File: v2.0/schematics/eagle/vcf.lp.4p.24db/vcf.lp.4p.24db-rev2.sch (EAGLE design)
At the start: 83 parts, among them IC1 TL082P, IC2 TL084P, IC3 TL084P, IC4 LM13700N, IC5 LM13700N, J1 IN, J2 OUT, T1 2N3904, T2 2N3904, T3 2N3906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

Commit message: VCFLP - updated rev3 with zenner clipping
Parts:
- added D2, D3: 1N5232B, _common:1N5232B
- R25: value 27K -> 100K
- R27: value 10K -> 68K
- RV3: value 10K (B) -> 250K (B)
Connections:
- new net N$35: D2.C, D3.C
- net 0V: now also D3.A
- net N$47: now also D2.A
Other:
- note added: "Alternative: R27 = 3.3K, RV3 = 10K"
- note added: "CUTOFF INIT"
- note added: "Option: - Res Boost switch isn't really that useful -- Hardwire res in to IC2D pin 14 (max res) - Use switch to select 4 pole / 2 pole -- Switch C12 between IC3A pin 1 and IC3C pin 8"
- note added: "Option: Add attenuverter"
- note removed: "ADD ATTENUVERTER"
- note removed: "Add trimmer to R16 (20K) to boost up to 25K to clip resonance overload"
- note removed: "FREQ INIT"
- note removed: "May want to set R8 to 200K, and boost the output R43 to 200K"
- note removed: "Note: The board traces need to be swapped for the cuttoff pins 2 and 3. Even though th schem is correct, the board mapping seems to have been broken for these two pins."
- note removed: "R27 to 3.3K (or 68K with VB3 at 250K) R25 to 100K Pair of Zenners from pin 7 to 0V to introduce clipping on REZ."
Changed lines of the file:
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@@
 <grid distance="0.1" unitdist="inch" unit="inch" style="lines" multiple="1" display="no" altdistance="0.01" altunitdist="inch" altunit="inch"/>
 <layers>
-<layer number="1" name="Top" color="4" fill="1" visible="no" active="no"/>
-<layer number="16" name="Bottom" color="1" fill="1" visible="no" active="no"/>
-<layer number="17" name="Pads" color="2" fill="1" visible="no" active="no"/>
-<layer number="18" name="Vias" color="2" fill="1" visible="no" active="no"/>
-<layer number="19" name="Unrouted" color="6" fill="1" visible="no" active="no"/>
-<layer number="20" name="Dimension" color="24" fill="1" visible="no" active="no"/>
-<layer number="21" name="tPlace" color="7" fill="1" visible="no" active="no"/>
-<layer number="22" name="bPlace" color="7" fill="1" visible="no" active="no"/>
-<layer number="23" name="tOrigins" color="15" fill="1" visible="no" active="no"/>
-<layer number="24" name="bOrigins" color="15" fill="1" visible="no" active="no"/>
-<layer number="25" name="tNames" color="7" fill="1" visible="no" active="no"/>
-<layer number="26" name="bNames" color="7" fill="1" visible="no" active="no"/>
-<layer number="27" name="tValues" color="7" fill="1" visible="no" active="no"/>
-<layer number="28" name="bValues" color="7" fill="1" visible="no" active="no"/>
+<layer number="1" name="Top" color="4" fill="1" visible="yes" active="no"/>
+<layer number="16" name="Bottom" color="1" fill="1" visible="yes" active="no"/>
+<layer number="17" name="Pads" color="2" fill="1" visible="yes" active="no"/>
+<layer number="18" name="Vias" color="2" fill="1" visible="yes" active="no"/>
+<layer number="19" name="Unrouted" color="6" fill="1" visible="yes" active="no"/>
+<layer number="20" name="Dimension" color="24" fill="1" visible="yes" active="no"/>
+<layer number="21" name="tPlace" color="7" fill="1" visible="yes" active="no"/>
+<layer number="22" name="bPlace" color="7" fill="1" visible="yes" active="no"/>
+<layer number="23" name="tOrigins" color="15" fill="1" visible="yes" active="no"/>
+<layer number="24" name="bOrigins" color="15" fill="1" visible="yes" active="no"/>
+<layer number="25" name="tNames" color="7" fill="1" visible="yes" active="no"/>
+<layer number="26" name="bNames" color="7" fill="1" visible="yes" active="no"/>
+<layer number="27" name="tValues" color="7" fill="1" visible="yes" active="no"/>
+<layer number="28" name="bValues" color="7" fill="1" visible="yes" active="no"/>
 <layer number="29" name="tStop" color="7" fill="3" visible="no" active="no"/>
 <layer number="30" name="bStop" color="7" fill="6" visible="no" active="no"/>
@@
 <layer number="35" name="tGlue" color="7" fill="4" visible="no" active="no"/>
 <layer number="36" name="bGlue" color="7" fill="5" visible="no" active="no"/>
-<layer number="37" name="tTest" color="7" fill="1" visible="no" active="no"/>
-<layer number="38" name="bTest" color="7" fill="1" visible="no" active="no"/>
+<layer number="37" name="tTest" color="7" fill="1" visible="yes" active="no"/>
+<layer number="38" name="bTest" color="7" fill="1" visible="yes" active="no"/>
 <layer number="39" name="tKeepout" color="4" fill="11" visible="no" active="no"/>
 <layer number="40" name="bKeepout" color="1" fill="11" visible="no" active="no"/>
@@
 <layer number="44" name="Drills" color="7" fill="1" visible="no" active="no"/>
 <layer number="45" name="Holes" color="7" fill="1" visible="no" active="no"/>
-<layer number="46" name="Milling" color="3" fill="1" visible="no" active="no"/>
-<layer number="47" name="Measures" color="7" fill="1" visible="no" active="no"/>
-<layer number="48" name="Document" color="7" fill="1" visible="no" active="no"/>
-<layer number="49" name="Reference" color="7" fill="1" visible="no" active="no"/>
-<layer number="50" name="dxf" color="7" fill="1" visible="no" active="no"/>
-<layer number="51" name="tDocu" color="7" fill="1" visible="no" active="no"/>
-<layer number="52" name="bDocu" color="7" fill="1" visible="no" active="no"/>
+<layer number="46" name="Milling" color="3" fill="1" visible="yes" active="no"/>
+<layer number="47" name="Measures" color="7" fill="1" visible="yes" active="no"/>
+<layer number="48" name="Document" color="7" fill="1" visible="yes" active="no"/>
+<layer number="49" name="Reference" color="7" fill="1" visible="yes" active="no"/>
+<layer number="50" name="dxf" color="7" fill="1" visible="yes" active="no"/>
+<layer number="51" name="tDocu" color="7" fill="1" visible="yes" active="no"/>
+<layer number="52" name="bDocu" color="7" fill="1" visible="yes" active="no"/>
 <layer number="88" name="SimResults" color="9" fill="1" visible="yes" active="yes"/>
 <layer number="89" name="SimProbes" color="9" fill="1" visible="yes" active="yes"/>
@@
 <part name="R6" library="resistor" deviceset="R-US_" device="0207/7" value="100K"/>
 <part name="GND30" library="supply1" library_urn="urn:adsk.eagle:library:371" deviceset="0V" device=""/>
-<part name="R27" library="resistor" deviceset="R-US_" device="0207/7" value="10K"/>
-<part name="R25" library="resistor" deviceset="R-US_" device="0207/7" value="27K"/>
+<part name="R27" library="resistor" deviceset="R-US_" device="0207/7" value="68K"/>
+<part name="R25" library="resistor" deviceset="R-US_" device="0207/7" value="100K"/>
 <part name="RV2" library="_common" deviceset="R-VAR" device="R-VAR-10" value="250K (B)"/>
 <part name="GND36" library="supply1" library_urn="urn:adsk.eagle:library:371" deviceset="0V" device=""/>
@@
 <part name="GND38" library="supply1" library_urn="urn:adsk.eagle:library:371" deviceset="0V" device=""/>
 <part name="R4" library="resistor" deviceset="R-US_" device="0207/7" value="100K"/>
-<part name="RV3" library="_common" deviceset="R-VAR" device="R-VAR-10" value="10K (B)"/>
+<part name="RV3" library="_common" deviceset="R-VAR" device="R-VAR-10" value="250K (B)"/>
 <part name="IC2" library="linear" library_urn="urn:adsk.eagle:library:262" deviceset="TL084" device="P" package3d_urn="urn:adsk.eagle:package:16407/2"/>
+<part name="D2" library="_common" deviceset="1N5232B" device=""/>
+<part name="D3" library="_common" deviceset="1N5232B" device=""/>
+<part name="GND15" library="supply1" library_urn="urn:adsk.eagle:library:371" deviceset="0V" device=""/>
 </parts>
 <sheets>
@@
 https://musicfromouterspace.com/analogsynth_new/VCFJAN2006/VCFJAN2006.html</text>
 <text x="5.08" y="55.88" size="1.778" layer="97">CUTOFF</text>
-<text x="33.02" y="22.86" size="1.778" layer="97">FREQ INIT</text>
+<text x="33.02" y="22.86" size="1.778" layer="97">CUTOFF INIT</text>
 <text x="33.02" y="78.74" size="1.778" layer="97">CV ATT</text>
 <text x="215.9" y="162.56" size="1.778" layer="97">RES</text>
-<text x="25.4" y="86.36" size="1.778" layer="91">ADD ATTENUVERTER</text>
-<text x="88.9" y="137.16" size="1.778" layer="91">Add trimmer to R16 (20K)
-to boost up to 25K to clip
-resonance overload</text>
-<text x="231.14" y="81.28" size="1.778" layer="91">Ideally, match the 4 transistors
+<text x="25.4" y="86.36" size="1.778" layer="97">Option: Add attenuverter</text>
+<text x="231.14" y="81.28" size="1.778" layer="97">Ideally, match the 4 transistors
 feeding the LM13700s</text>
-<text x="-43.18" y="38.1" size="1.778" layer="91">Note: The board traces need to be swapped
-for the cuttoff pins 2 and 3.
-Even though th schem is correct, the board
-mapping seems to have been broken for these two pins.</text>
-<text x="55.88" y="134.62" size="1.778" layer="91">May want to set R8 to 200K,
-and boost the output
-R43 to 200K</text>
-<text x="190.5" y="149.86" size="1.778" layer="91">R27 to 3.3K (or 68K with VB3 at 250K)
-R25 to 100K
-Pair of Zenners from pin 7 to
-0V to introduce clipping on REZ.</text>
+<text x="236.22" y="162.56" size="1.778" layer="97">Alternative: R27 = 3.3K, RV3 = 10K</text>
+<text x="281.94" y="154.94" size="1.778" layer="97">Option:
+- Res Boost switch isn't really that useful
+-- Hardwire res in to IC2D pin 14 (max res)
+- Use switch to select 4 pole / 2 pole
+-- Switch C12 between IC3A pin 1 and IC3C pin 8</text>
 </plain>
 <instances>
@@
 </instance>
 <instance part="IC2" gate="P" x="419.1" y="35.56" smashed="yes"/>
+<instance part="D2" gate="G$1" x="226.06" y="139.7" smashed="yes" rot="R270">
+<attribute name="NAME" x="223.4946" y="139.7" size="1.778" layer="95" rot="R270" align="center"/>
+<attribute name="VALUE" x="221.4626" y="139.7" size="1.778" layer="96" rot="R270" align="center"/>
+</instance>
+<instance part="D3" gate="G$1" x="226.06" y="134.62" smashed="yes" rot="R90">
+<attribute name="NAME" x="228.6254" y="134.62" size="1.778" layer="95" rot="R90" align="center"/>
+<attribute name="VALUE" x="230.6574" y="134.62" size="1.778" layer="96" rot="R90" align="center"/>
+</instance>
+<instance part="GND15" gate="1" x="226.06" y="129.54" smashed="yes">
+<attribute name="VALUE" x="224.155" y="127" size="1.778" layer="96"/>
+</instance>
 </instances>
 <busses>
@@
 <wire x1="452.12" y1="109.22" x2="452.12" y2="106.68" width="0.1524" layer="91"/>
 </segment>
+<segment>
+<pinref part="D3" gate="G$1" pin="A"/>
+<pinref part="GND15" gate="1" pin="0V"/>
+</segment>
 </net>
 <net name="+12V" class="1">
@@
 <wire x1="226.06" y1="144.78" x2="226.06" y2="152.4" width="0.1524" layer="91"/>
 <junction x="226.06" y="144.78"/>
+<pinref part="D2" gate="G$1" pin="A"/>
+<wire x1="226.06" y1="144.78" x2="226.06" y2="142.24" width="0.1524" layer="91"/>
 </segment>
 </net>
@@
 </segment>
 </net>
+<net name="N$35" class="0">
+<segment>
+<pinref part="D2" gate="G$1" pin="C"/>
+<pinref part="D3" gate="G$1" pin="C"/>
+</segment>
+</net>

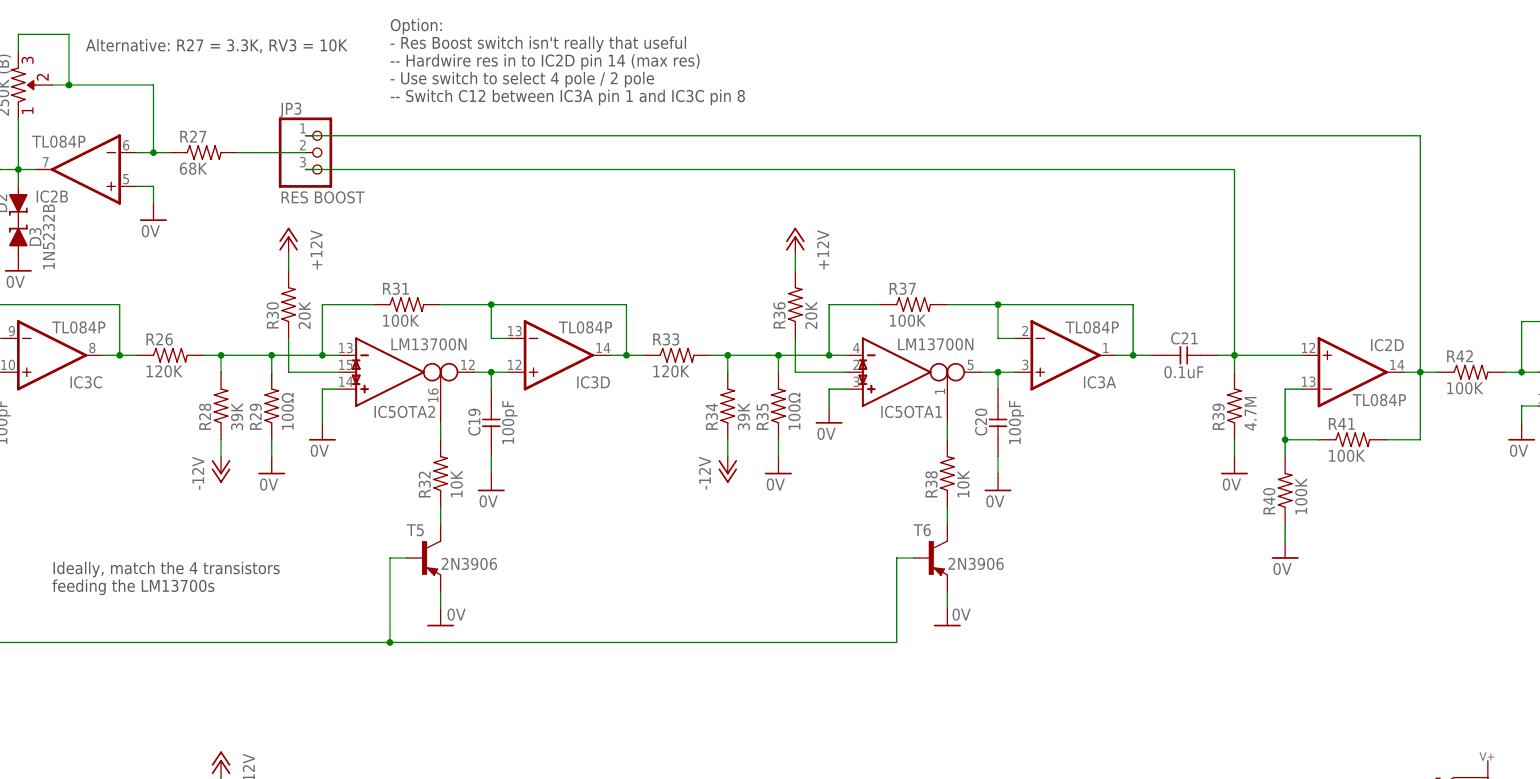
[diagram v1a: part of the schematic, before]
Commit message: VFCLP: Changed RES++ switch into 2/4 Pole select switch
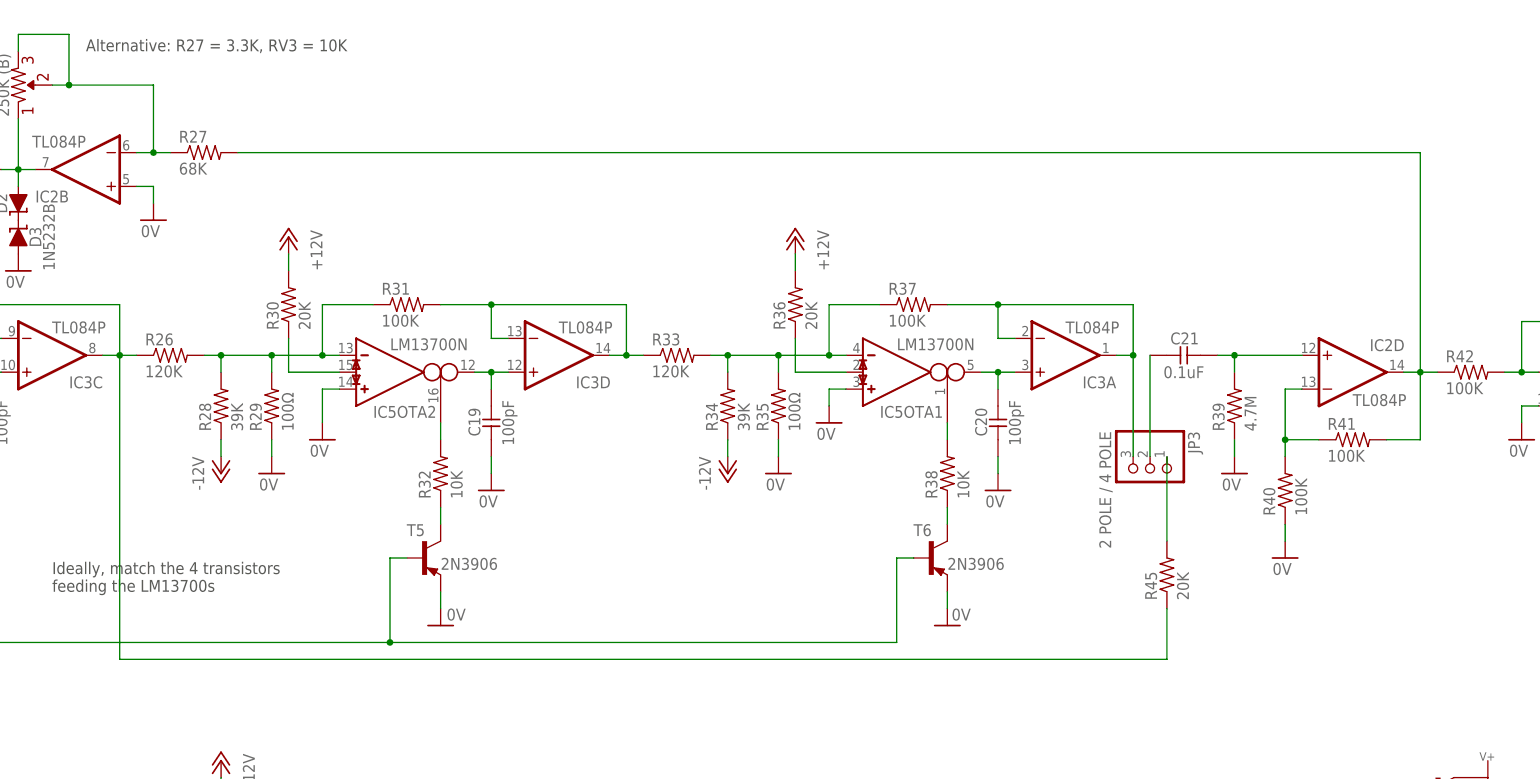
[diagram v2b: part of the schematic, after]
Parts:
- added R45: 20K, resistor:R-US_0207/7
- JP3: value RES BOOST -> 2 POLE / 4 POLE
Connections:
- removed net N$40: JP3.2, R27.2
- new net N$36: C21.2, JP3.2
- new net N$37: JP3.1, R45.2
- net N$25: now also R45.1
- net N$39: no longer JP3.3
- net N$43: now also R27.2; no longer JP3.1
- net N$65: now also JP3.3; no longer C21.2
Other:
- note removed: "Option: - Res Boost switch isn't really that useful -- Hardwire res in to IC2D pin 14 (max res) - Use switch to select 4 pole / 2 pole -- Switch C12 between IC3A pin 1 and IC3C pin 8"
- moved on the sheet: JP3
